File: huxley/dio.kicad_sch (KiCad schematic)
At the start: 1 part, among them J33 67996-130HLF

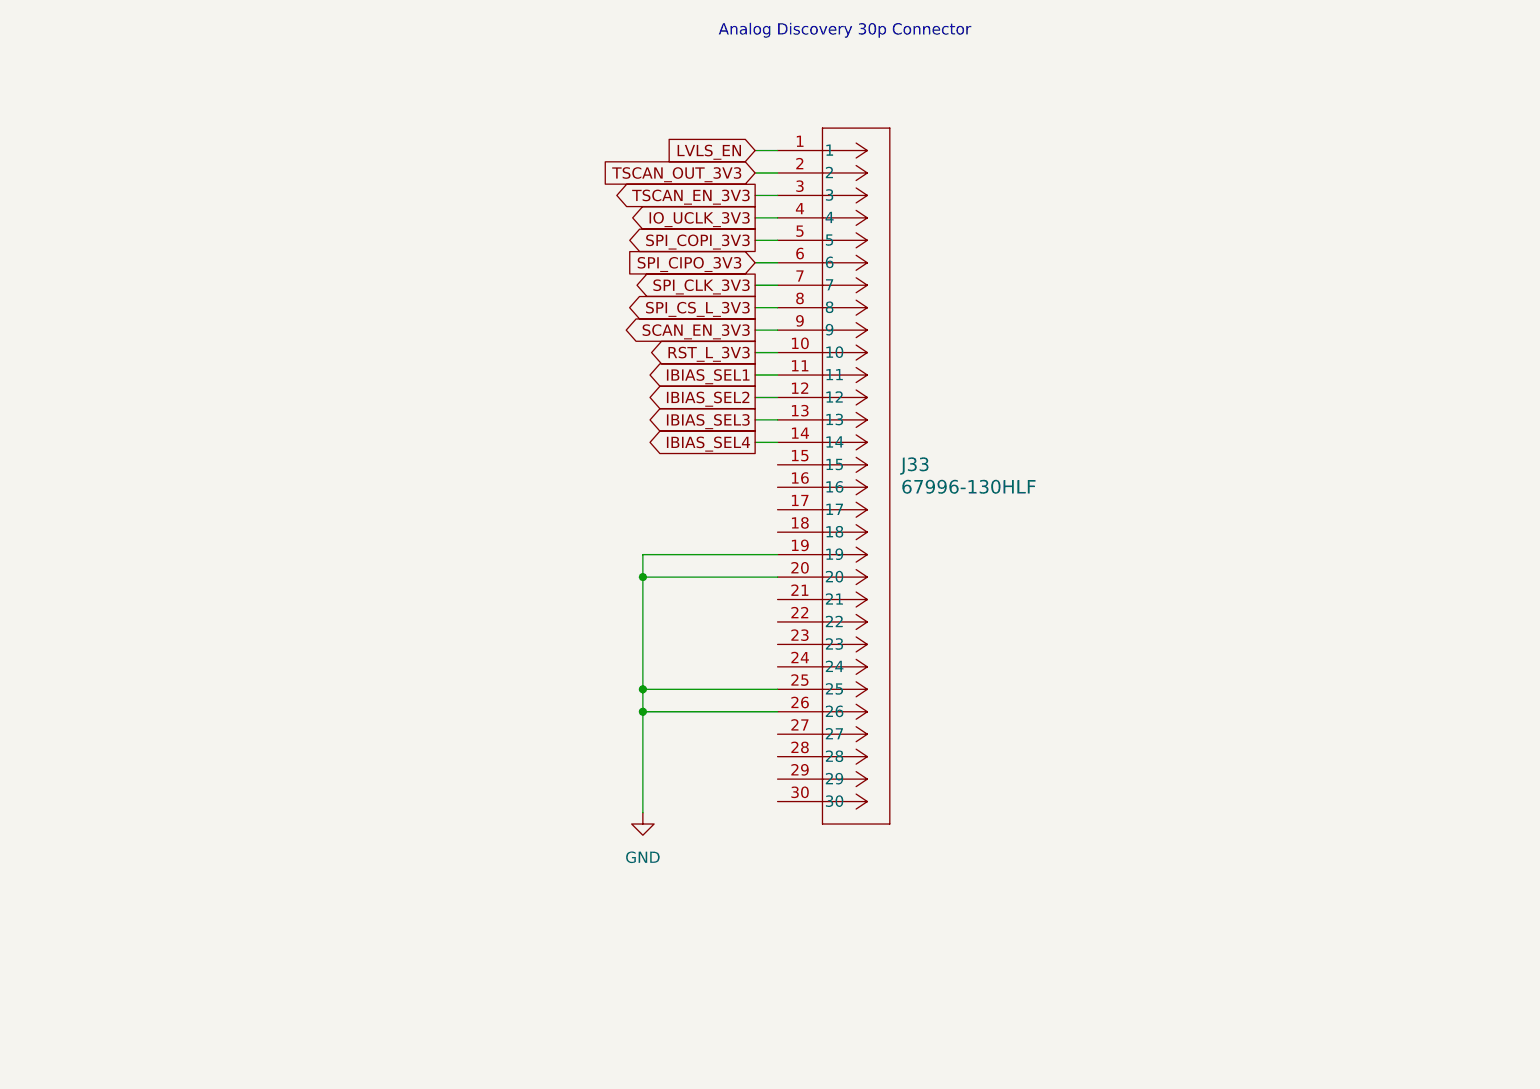
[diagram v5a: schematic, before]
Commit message: fixed all bad refs; replaced analog discovery connector; change level shifter 3v3 to from analog discovery
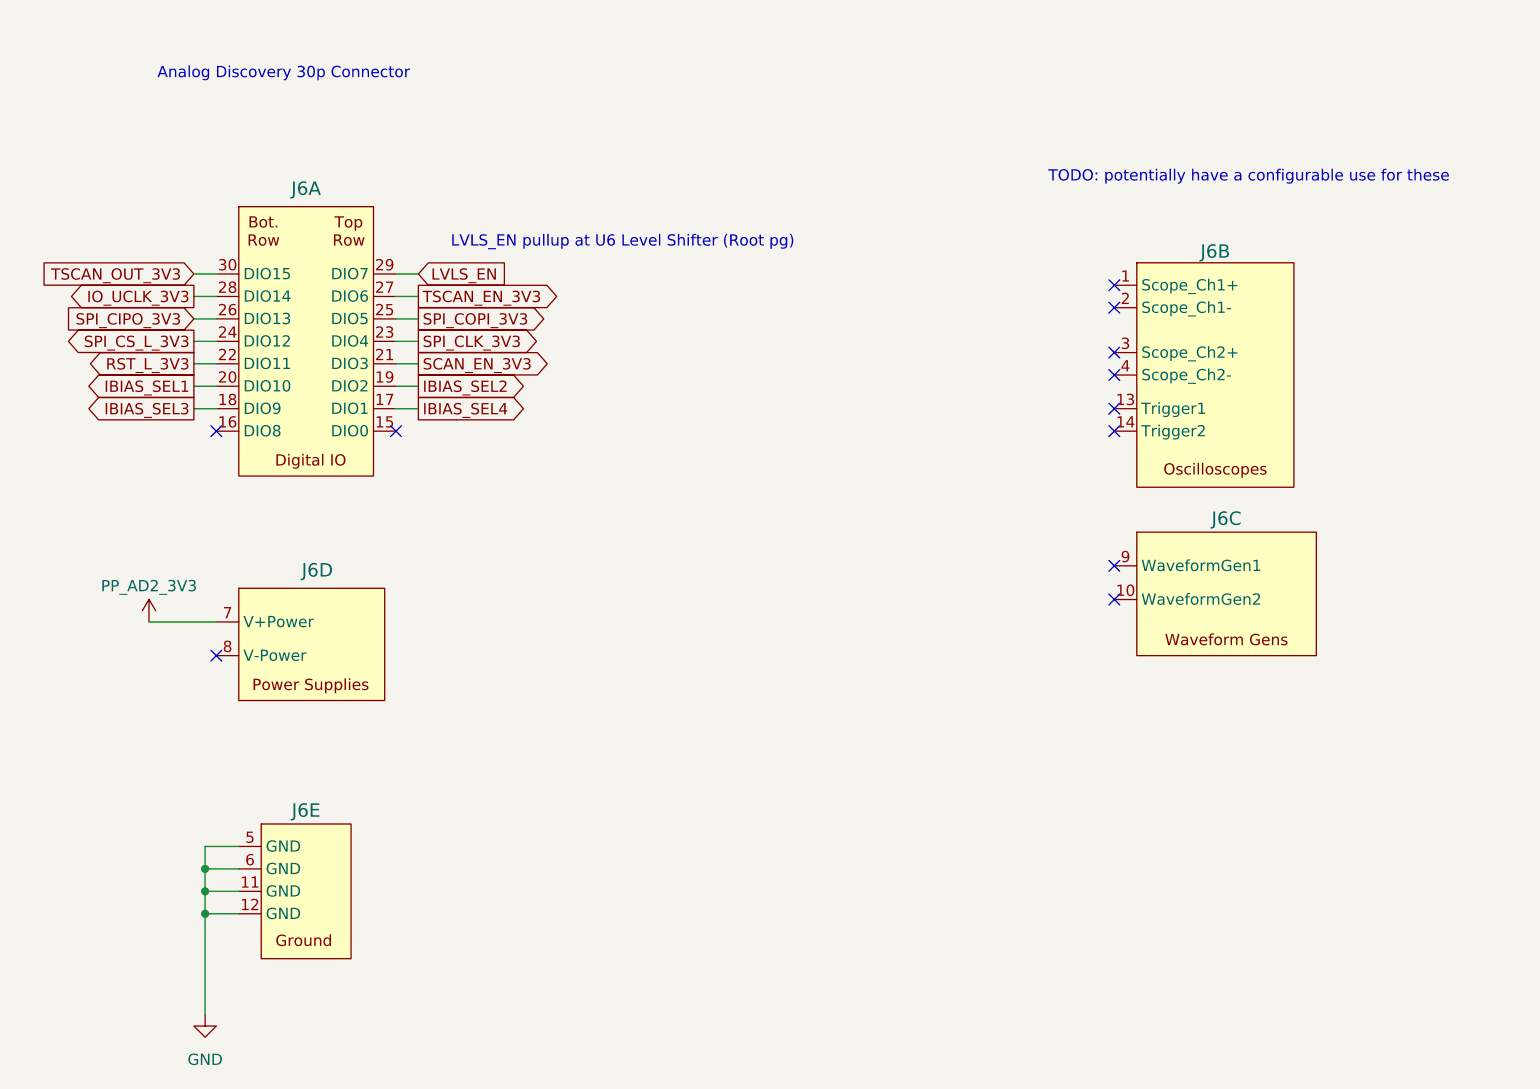
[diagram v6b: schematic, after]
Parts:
- removed J33: 67996-130HLF, 726_footprints:30p_connector, symbol _PHASE:67996-130HLF
- added J6: ~, Connector_PinHeader_2.54mm:PinHeader_2x15_P2.54mm_Horizontal, symbol 0_PHASE:ANALOG_DISCOVERY_30P
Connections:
- net GND: now also J6.11 (GND), J6.12 (GND), J6.5 (GND), J6.6 (GND)
- net IBIAS_SEL1: now also J6.20 (DIO10)
- net IBIAS_SEL2: now also J6.19 (DIO2)
- net IBIAS_SEL3: now also J6.18 (DIO9)
- net IBIAS_SEL4: now also J6.17 (DIO1)
- net IO_UCLK_3V3: now also J6.28 (DIO14)
- net LVLS_EN: now also J6.29 (DIO7)
- net RST_L_3V3: now also J6.22 (DIO11)
- net SCAN_EN_3V3: now also J6.21 (DIO3)
- net SPI_CIPO_3V3: now also J6.26 (DIO13)
- net SPI_CLK_3V3: now also J6.23 (DIO4)
- net SPI_COPI_3V3: now also J6.25 (DIO5)
- net SPI_CS_L_3V3: now also J6.24 (DIO12)
- net TSCAN_EN_3V3: now also J6.27 (DIO6)
- net TSCAN_OUT_3V3: now also J6.30 (DIO15)
- new net PP_AD2_3V3: J6.7 (V+Power)
- no-connect marks 0 -> 11
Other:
- note added: "LVLS_EN pullup at U6 Level Shifter (Root pg)"
- note added: "TODO: potentially have a configurable use for these"

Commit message: pre edgechange
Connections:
- net IBIAS_SEL1: now also J6.18 (DIO9); no longer J6.20 (DIO10)
- net IBIAS_SEL2: now also J6.17 (DIO1); no longer J6.19 (DIO2)
- net IBIAS_SEL3: now also J6.20 (DIO10); no longer J6.18 (DIO9)
- net IBIAS_SEL4: now also J6.19 (DIO2); no longer J6.17 (DIO1)
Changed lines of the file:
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@@
-		)
-	)
-	(global_label "IBIAS_SEL1"
-		(shape output)
-		(at 76.2 77.47 180)
-		(fields_autoplaced yes)
-		(effects
-			(font
-				(size 1.27 1.27)
-			)
-			(justify right)
-		)
-		(property "Intersheetrefs" "${INTERSHEET_REFS}"
-			(at 62.8734 77.47 0)
-			(effects
-				(font
-					(size 1.27 1.27)
-				)
-				(justify right)
-				(hide yes)
-			)
 		)
 	)
@@
 					(size 1.27 1.27)
 				)
+				(hide yes)
+			)
+		)
+	)
+	(global_label "IBIAS_SEL4"
+		(shape output)
+		(at 101.6 77.47 0)
+		(fields_autoplaced yes)
+		(effects
+			(font
+				(size 1.27 1.27)
+			)
+			(justify left)
+		)
+		(property "Intersheetrefs" "${INTERSHEET_REFS}"
+			(at 114.9266 77.47 0)
+			(effects
+				(font
+					(size 1.27 1.27)
+				)
+				(justify left)
 				(hide yes)
 			)
@@
 		)
 	)
-	(global_label "IBIAS_SEL2"
-		(shape output)
-		(at 101.6 77.47 0)
-		(fields_autoplaced yes)
-		(effects
-			(font
-				(size 1.27 1.27)
-			)
-			(justify left)
-		)
-		(property "Intersheetrefs" "${INTERSHEET_REFS}"
-			(at 114.9266 77.47 0)
-			(effects
-				(font
-					(size 1.27 1.27)
-				)
-				(justify left)
-				(hide yes)
-			)
-		)
-	)
 	(global_label "RST_L_3V3"
 		(shape output)
@@
 		)
 	)
+	(global_label "IBIAS_SEL2"
+		(shape output)
+		(at 101.6 80.01 0)
+		(fields_autoplaced yes)
+		(effects
+			(font
+				(size 1.27 1.27)
+			)
+			(justify left)
+		)
+		(property "Intersheetrefs" "${INTERSHEET_REFS}"
+			(at 114.9266 80.01 0)
+			(effects
+				(font
+					(size 1.27 1.27)
+				)
+				(justify left)
+				(hide yes)
+			)
+		)
+	)
 	(global_label "IBIAS_SEL3"
 		(shape output)
+		(at 76.2 77.47 180)
+		(fields_autoplaced yes)
+		(effects
+			(font
+				(size 1.27 1.27)
+			)
+			(justify right)
+		)
+		(property "Intersheetrefs" "${INTERSHEET_REFS}"
+			(at 62.8734 77.47 0)
+			(effects
+				(font
+					(size 1.27 1.27)
+				)
+				(justify right)
+				(hide yes)
+			)
+		)
+	)
+	(global_label "IBIAS_SEL1"
+		(shape output)
 		(at 76.2 80.01 180)
 		(fields_autoplaced yes)
@@
 				(hide yes)
 			)
-		)
-	)
-	(global_label "IBIAS_SEL4"
-		(shape output)
-		(at 101.6 80.01 0)
-		(fields_autoplaced yes)
-		(effects
-			(font
-				(size 1.27 1.27)
-			)
-			(justify left)
-		)
-		(property "Intersheetrefs" "${INTERSHEET_REFS}"
-			(at 114.9266 80.01 0)
-			(effects
-				(font
-					(size 1.27 1.27)
-				)
-				(justify left)
-				(hide yes)
-			)
